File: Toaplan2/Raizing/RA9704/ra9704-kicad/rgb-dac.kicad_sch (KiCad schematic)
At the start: 11 parts, among them U610 74AC273, U611 74AC273

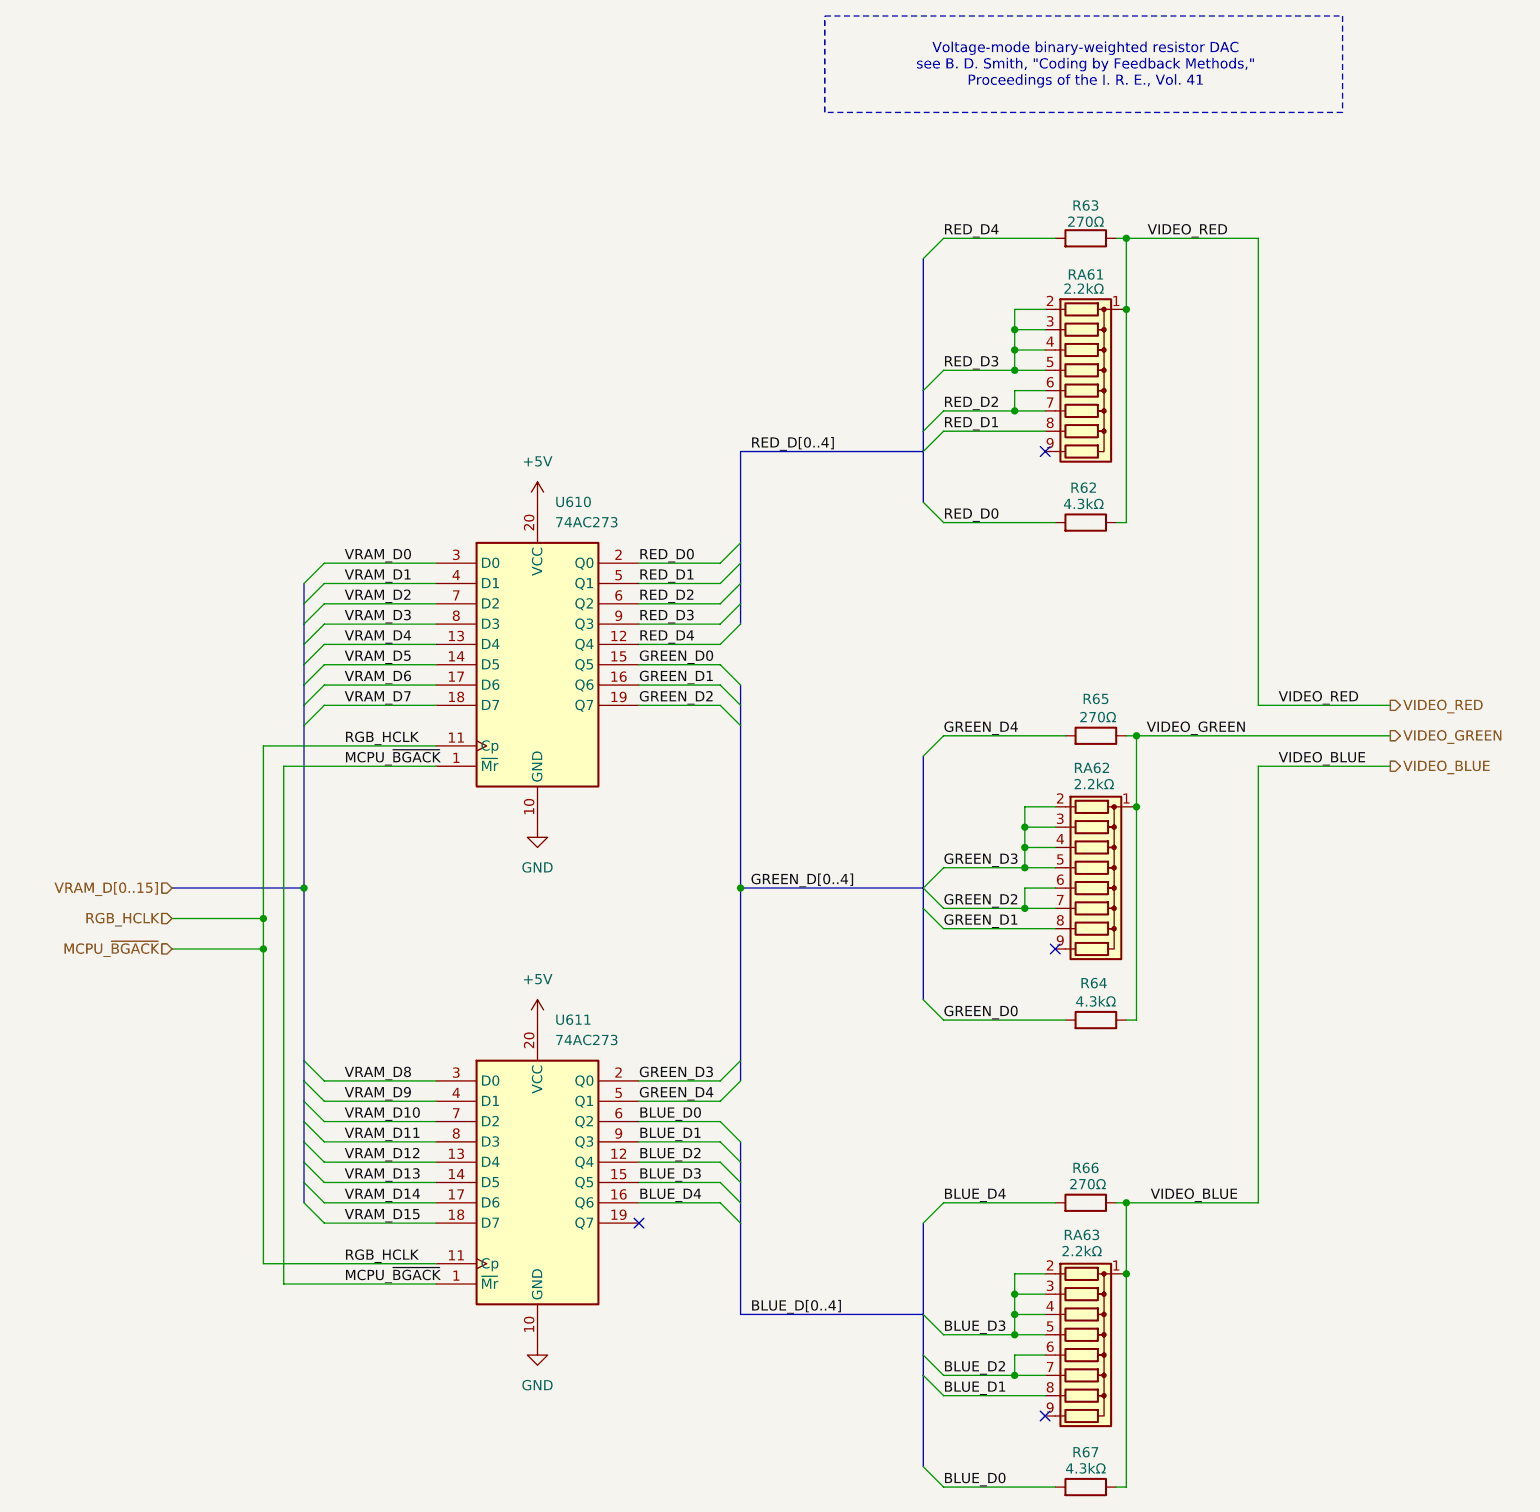
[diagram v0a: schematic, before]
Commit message: fix(ra9704): Add Os as a proxy for 0s in all reference designators
RA9704 has reference designators such that each number has a preceding zero (e.g. RA076, U074, etc.). This causes a bug in KiCAD.

This is 'fixed' by using the 'O' (the letter 'Oh') character instead.

For more info, see the following issue on the KiCAD Gitlab repo

https://gitlab.com/kicad/code/kicad/-/issues/19229
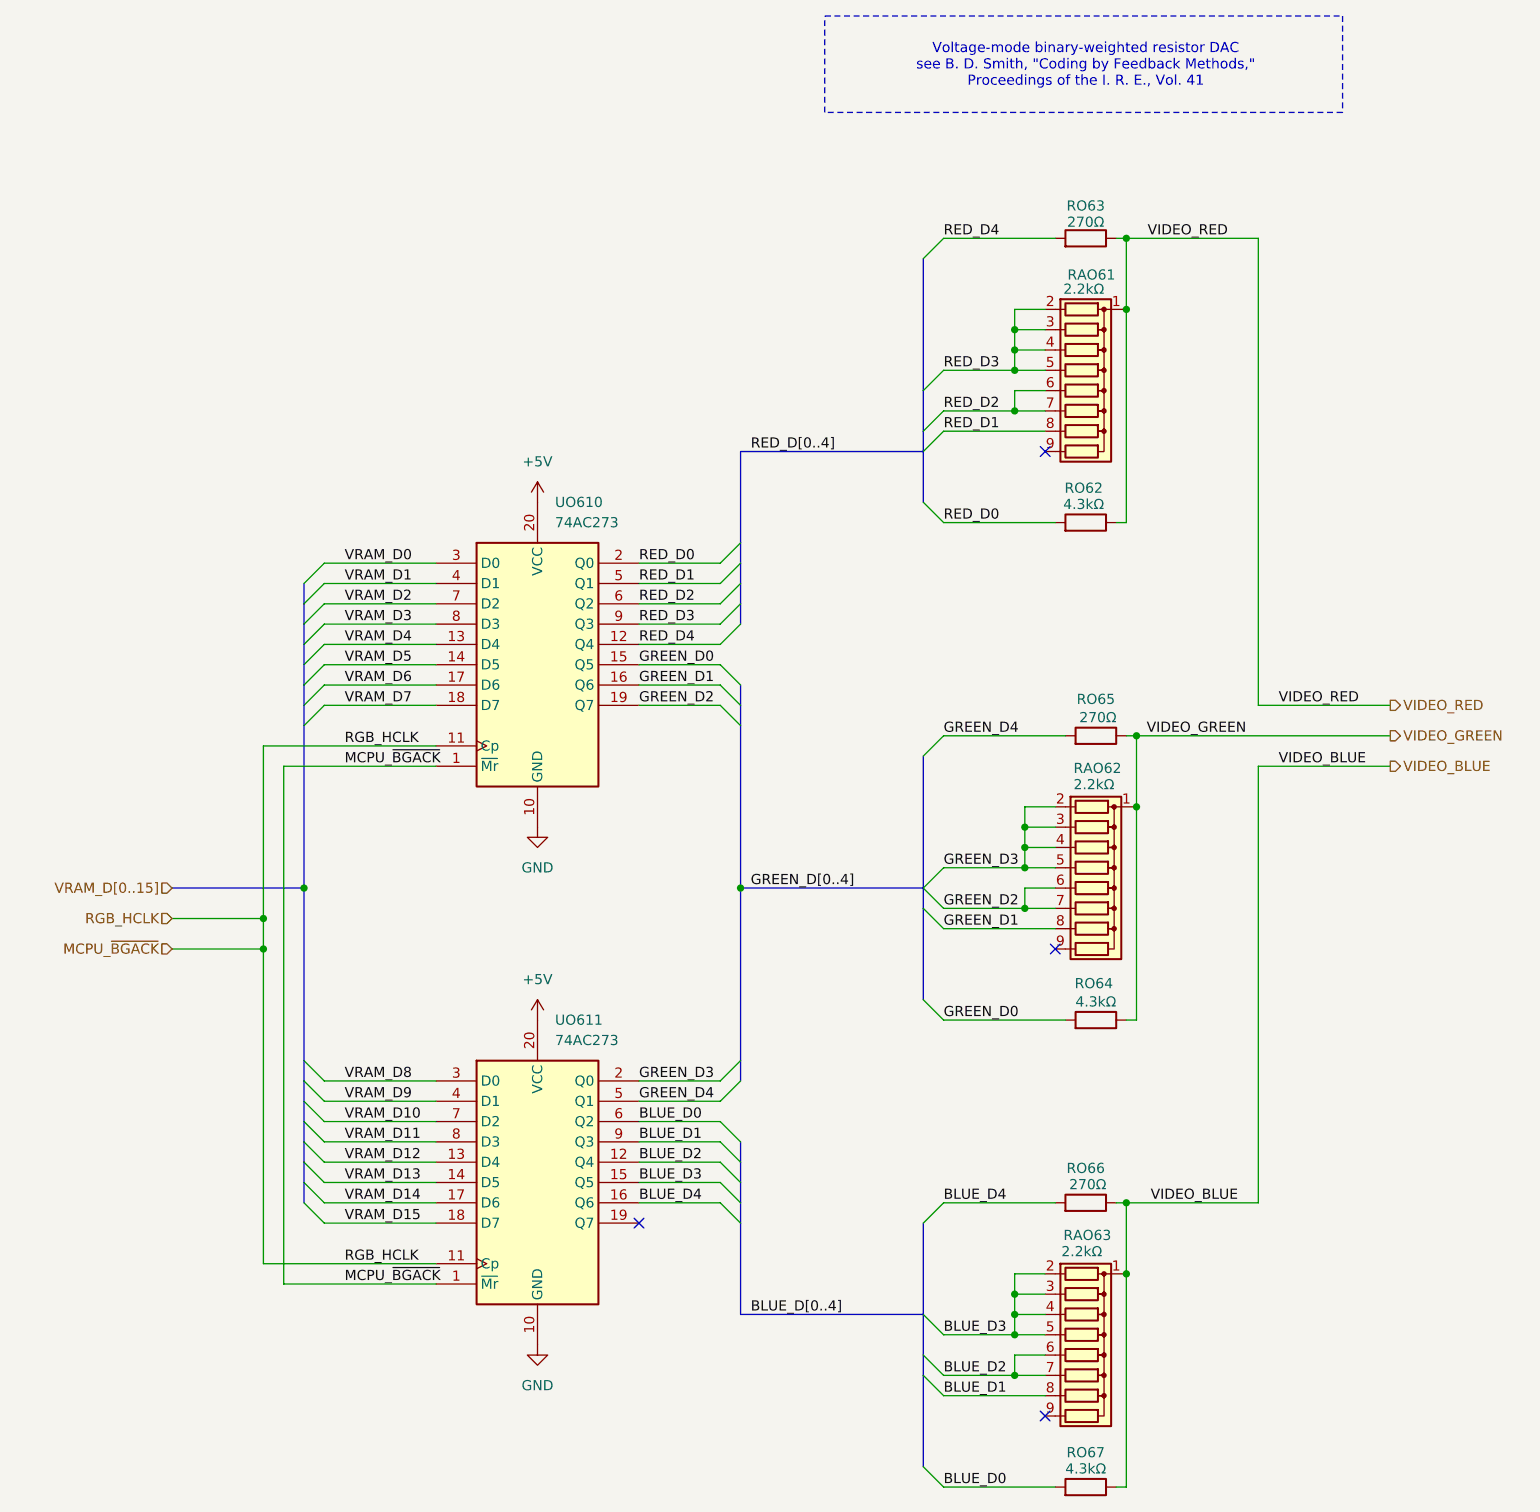
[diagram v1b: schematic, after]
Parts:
- renumbered RA61 to RAO61, RA62 to RAO62, RA63 to RAO63, R62 to RO62, R63 to RO63, R64 to RO64, R65 to RO65, R66 to RO66, R67 to RO67, U610 to UO610, U611 to UO611
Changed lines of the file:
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@@
 		(on_board yes)
 		(dnp no)
-		(property "Reference" "R62"
+		(property "Reference" "RO62"
 			(at 148.336 84.582 90)
 			(effects
@@
 			(project "ra9704"
 				(path "/24d3b4cf-2360-45fc-8c40-cedc8afdf9e1/50cd2f12-42ff-42bb-aa2d-370ff3056b6e"
-					(reference "R62")
+					(reference "RO62")
 					(unit 1)
 				)
@@
 		(on_board yes)
 		(dnp no)
-		(property "Reference" "R66"
+		(property "Reference" "RO66"
 			(at 148.59 169.672 90)
 			(effects
@@
 			(project "ra9704"
 				(path "/24d3b4cf-2360-45fc-8c40-cedc8afdf9e1/50cd2f12-42ff-42bb-aa2d-370ff3056b6e"
-					(reference "R66")
+					(reference "RO66")
 					(unit 1)
 				)
@@
 		(on_board yes)
 		(dnp no)
-		(property "Reference" "R67"
+		(property "Reference" "RO67"
 			(at 148.59 205.232 90)
 			(effects
@@
 			(project "ra9704"
 				(path "/24d3b4cf-2360-45fc-8c40-cedc8afdf9e1/50cd2f12-42ff-42bb-aa2d-370ff3056b6e"
-					(reference "R67")
+					(reference "RO67")
 					(unit 1)
 				)
@@
 		(dnp no)
 		(fields_autoplaced yes)
-		(property "Reference" "U611"
+		(property "Reference" "UO611"
 			(at 82.2041 151.13 0)
 			(effects
@@
 			(project "ra9704"
 				(path "/24d3b4cf-2360-45fc-8c40-cedc8afdf9e1/50cd2f12-42ff-42bb-aa2d-370ff3056b6e"
-					(reference "U611")
+					(reference "UO611")
 					(unit 1)
 				)
@@
 		(on_board yes)
 		(dnp no)
-		(property "Reference" "RA62"
+		(property "Reference" "RAO62"
 			(at 147.066 119.634 90)
 			(effects
@@
 			(project "ra9704"
 				(path "/24d3b4cf-2360-45fc-8c40-cedc8afdf9e1/50cd2f12-42ff-42bb-aa2d-370ff3056b6e"
-					(reference "RA62")
+					(reference "RAO62")
 					(unit 1)
 				)
@@
 		(on_board yes)
 		(dnp no)
-		(property "Reference" "R64"
+		(property "Reference" "RO64"
 			(at 149.606 146.558 90)
 			(effects
@@
 			(project "ra9704"
 				(path "/24d3b4cf-2360-45fc-8c40-cedc8afdf9e1/50cd2f12-42ff-42bb-aa2d-370ff3056b6e"
-					(reference "R64")
+					(reference "RO64")
 					(unit 1)
 				)
@@
 		(on_board yes)
 		(dnp no)
-		(property "Reference" "R65"
+		(property "Reference" "RO65"
 			(at 149.86 110.998 90)
 			(effects
@@
 			(project "ra9704"
 				(path "/24d3b4cf-2360-45fc-8c40-cedc8afdf9e1/50cd2f12-42ff-42bb-aa2d-370ff3056b6e"
-					(reference "R65")
+					(reference "RO65")
 					(unit 1)
 				)
@@
 		(on_board yes)
 		(dnp no)
-		(property "Reference" "RA61"
+		(property "Reference" "RAO61"
 			(at 146.304 57.912 90)
 			(effects
@@
 			(project "ra9704"
 				(path "/24d3b4cf-2360-45fc-8c40-cedc8afdf9e1/50cd2f12-42ff-42bb-aa2d-370ff3056b6e"
-					(reference "RA61")
+					(reference "RAO61")
 					(unit 1)
 				)
@@
 		(on_board yes)
 		(dnp no)
-		(property "Reference" "R63"
+		(property "Reference" "RO63"
 			(at 148.59 49.276 90)
 			(effects
@@
 			(project "ra9704"
 				(path "/24d3b4cf-2360-45fc-8c40-cedc8afdf9e1/50cd2f12-42ff-42bb-aa2d-370ff3056b6e"
-					(reference "R63")
+					(reference "RO63")
 					(unit 1)
 				)
@@
 		(on_board yes)
 		(dnp no)
-		(property "Reference" "RA63"
+		(property "Reference" "RAO63"
 			(at 145.796 178.054 90)
 			(effects
@@
 			(project "ra9704"
 				(path "/24d3b4cf-2360-45fc-8c40-cedc8afdf9e1/50cd2f12-42ff-42bb-aa2d-370ff3056b6e"
-					(reference "RA63")
+					(reference "RAO63")
 					(unit 1)
 				)
@@
 		(dnp no)
 		(fields_autoplaced yes)
-		(property "Reference" "U610"
+		(property "Reference" "UO610"
 			(at 82.2041 86.36 0)
 			(effects
@@
 			(project "ra9704"
 				(path "/24d3b4cf-2360-45fc-8c40-cedc8afdf9e1/50cd2f12-42ff-42bb-aa2d-370ff3056b6e"
-					(reference "U610")
-					(unit 1)
-				)
+					(reference "UO610")
+					(unit 1)
+				)
